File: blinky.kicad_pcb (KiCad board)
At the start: 2 copper layers, 25 x 25 mm, 7 parts, among them U1 7555

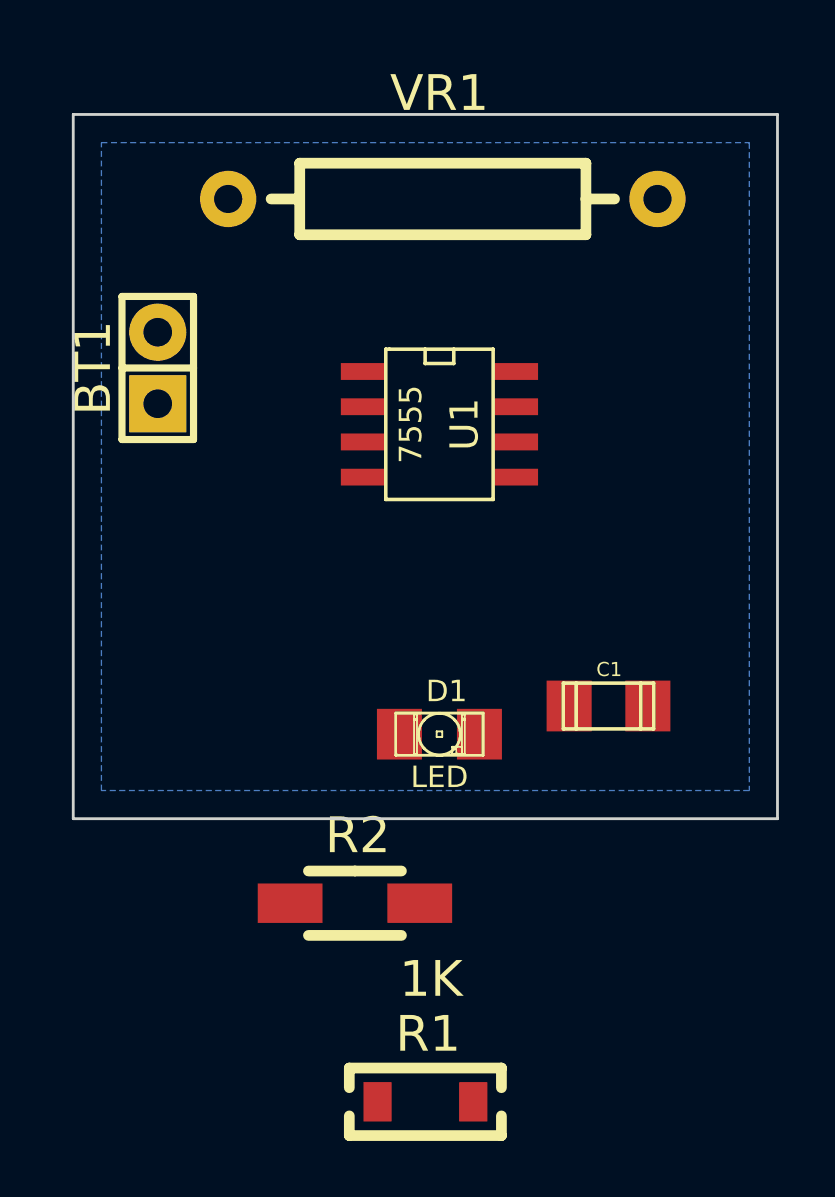
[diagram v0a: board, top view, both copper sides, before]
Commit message: PCB layout fixed, had ended up in a different file some
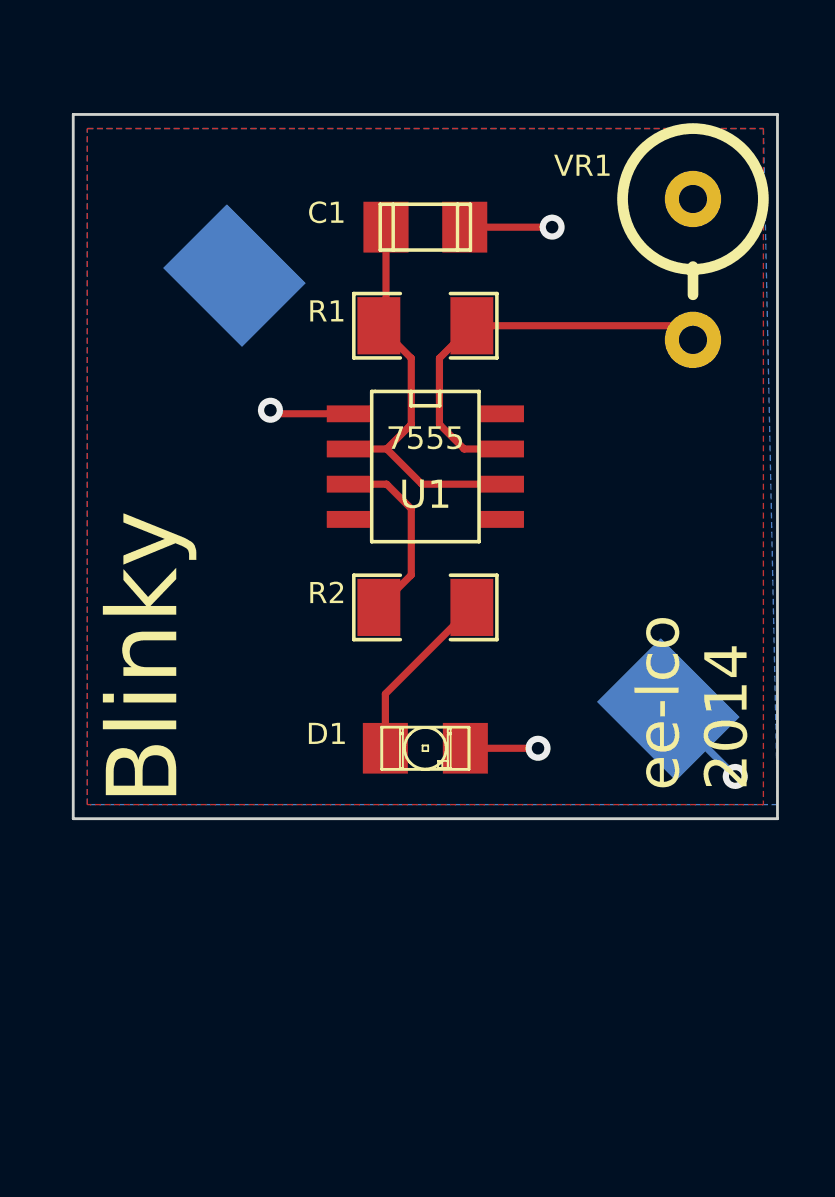
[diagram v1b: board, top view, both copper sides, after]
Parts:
- BT1: footprint Pin_Headers:Pin_Header_Straight_1x02 -> Blinky:CR2032; moved to B.Cu
- R1: footprint Resistors_SMD:Resistor_SMD1206_ReflowWave_RevA_Date21Jun2010 -> SMD_Packages:SM1206
- R2: footprint Resistors_SMD:Resistor_SMD1206_HandSoldering_RevA_Date21Jun2010 -> SMD_Packages:SM1206
- VR1: footprint Resistors_ThroughHole:Resistor_Horizontal_RM15mm_22Apr2011 -> Resistors_ThroughHole:Resistor_Vertical_RM5mm_22Apr2011
- moved R1 27.6 mm to (142.5, 92.5), turned to 180 degrees
- moved C1 18.2 mm to (142.5, 89.0), turned to 180 degrees
- moved BT1 11.4 mm to (143.5, 98.5), turned to 225 degrees
- moved R2 10.8 mm to (142.5, 102.5)
- moved VR1 9.34 mm to (152.0, 90.5), turned to 270 degrees
- moved U1 1.58 mm to (142.5, 97.5)
- moved D1 0.71 mm to (142.5, 107.5)
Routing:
- net Net-(R1-Pad1): track 0.00 -> 14.6 mm
- net Net-(C1-Pad1): track 0.00 -> 14.5 mm
- net GND: track 0.00 -> 8.53 mm, vias 0 -> 3
- net Net-(R2-Pad1): track 0.00 -> 6.54 mm
- net Net-(D1-Pad1): track 0.00 -> 6.27 mm
- net VCC: track 0.00 -> 3.36 mm, vias 0 -> 1
- added copper zone on F.Cu, net VCC
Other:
- board text added: "Blinky"
- board text added: "ee-lco 2014"
